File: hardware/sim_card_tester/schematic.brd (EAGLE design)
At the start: 160 x 101.6 mm, 140 parts, among them IC1 TPS6300, J1 CON_MICRO_SDDM3AT-SF-PEJM5, J2 MICRO_USB_B_HIROSE_ZX62R-B-5P, J3 NANO_SIM, J4 NANO_SIM, J5 NANO_SIM, J6 NANO_SIM, J7 TC2030-JLINK-L, J8 U.FL-R-SMT, Q1 MOSFET-NCHANNELSMD, Q2 MOSFET-NCHANNELSMD, Q3 MOSFET-NCHANNELSMD, Q4 SI223DDS, U1 AB1815-T3, U10 SIP32510, U11 SIP32510, U12 UBLOX_SARA_G350, U13 TXB0104RUT, U15 MAX4734EUB+, U2 BGA725L6-ALT, U20 MAX4734EUB+, U21 MAX4734EUB+, U22 MAX4734EUB+, U3 FTDI234XD, U4 SAFFB1G56KB0F0A, U5 MAX8887EZK33+T, U6 MCP73831, U7 MAX-M8, U8 MAX67XXMAX6749MAX67XX, U9 NRF52840, X1 ABS07-32.768KHZ-7-T, X4 32MHz, X5 32.768kHz

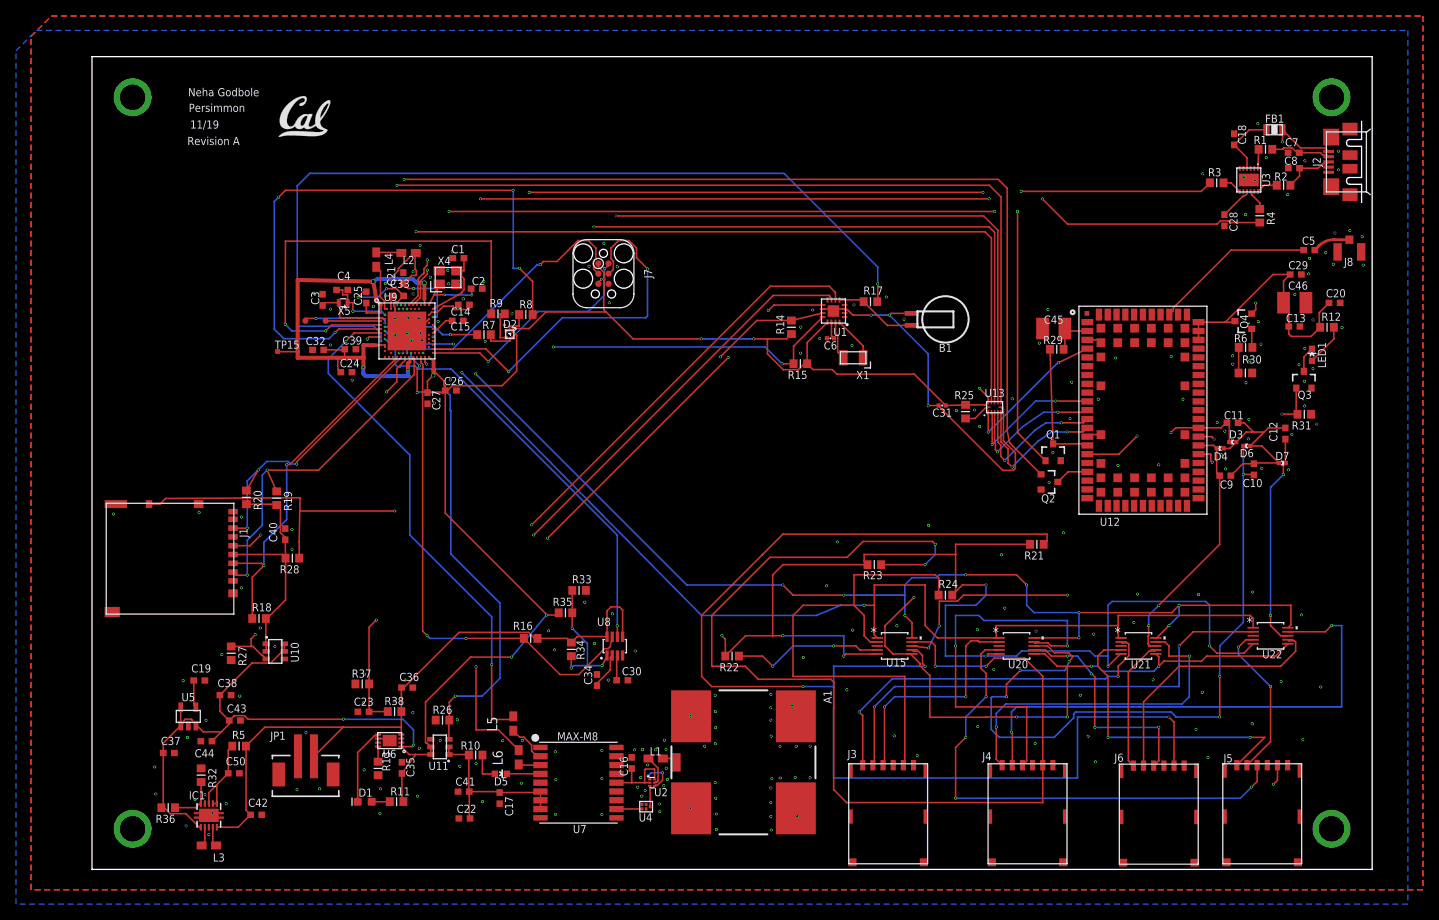
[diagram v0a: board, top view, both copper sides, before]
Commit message: fixed numbering
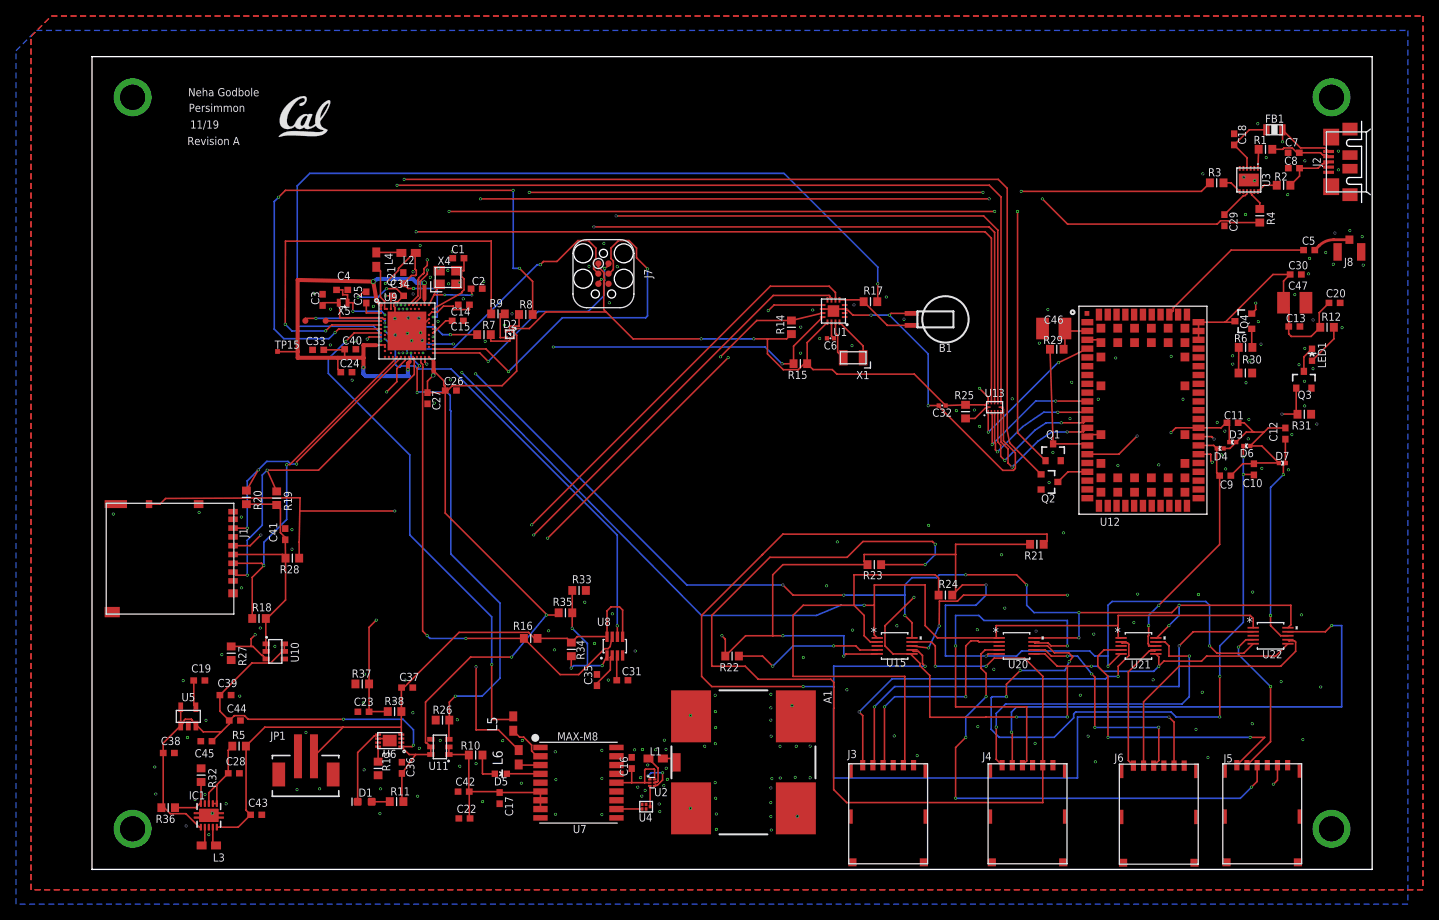
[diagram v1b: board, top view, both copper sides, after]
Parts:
- removed C50: .1uF, Nordic_nRF:RESC0603_L
- added C47: 220uF, BeagleBone_Black_Wireless:C1210
- C28: value 100nF -> .1uF
- C30: value 0.82uF -> 100nF
- C31: value 1uF -> 0.82uF; device passives:0402_CAP -> Nordic_nRF:RESC0603_L
- C32: device Nordic_nRF:RESC0603_L -> passives:0402_CAP
- C34: value 2.2uF -> 1uF
- C35: value 4.7uF -> 2.2uF
- C41: value 10uF -> 4.7uF
- C45: value 100uF -> 10uF; device BeagleBone_Black_Wireless:C1210 -> Nordic_nRF:RESC0603_L
- C46: value 220uF -> 100uF
- moved C28 141.8 mm to (17.7, 12.0), turned to 0 degrees
- moved C45 117.8 mm to (14.3, 16.0)
- moved C30 98.3 mm to (150.5, 74.4)
- moved C32 78.3 mm to (106.3, 58.0)
- moved C34 54.1 mm to (38.3, 71.7), turned to 0 degrees
- moved C31 52.7 mm to (66.3, 23.6), turned to 0 degrees
- moved C39 46.0 mm to (16.7, 21.8)
- moved C41 39.2 mm to (24.2, 41.9), turned to 90 degrees
- moved C37 30.9 mm to (39.4, 22.7)
- moved C46 30.3 mm to (120.2, 67.6), turned to 180 degrees
- moved C35 26.7 mm to (63.1, 23.7)
- moved C42 26.1 mm to (46.5, 9.73)
- moved C40 24.5 mm to (32.3, 65.0), turned to 0 degrees
- moved C43 12.1 mm to (20.5, 6.83)
- moved C33 12.1 mm to (28.3, 64.9), turned to 180 degrees
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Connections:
- net +3V3: now also C33.1, C36.1, C40.1, C45.1; no longer C31.1, C35.1, C37.1, C43.1
- net BAT: now also C37.1, C43.1; no longer C36.1, C42.1
- net GND: now also C41.2, C42.1, C47.2; no longer C41.1, C42.2, C50.2
- net GPS_VCC: now also C42.2; no longer C41.2
- net GSM_GATED: now also C30.1, C47.1; no longer C29.1, C46.1
- net N$16: now also C46.1; no longer C45.1
- net N$29: now also C28.1; no longer C50.1
- net N$32: now also C34.1; no longer C33.1
- net N$36: now also C31.1; no longer C30.1
- net N$39: now also C35.1; no longer C34.1
- net N$55: now also C41.1; no longer C40.1
- net VCC_LINUX_1V8: now also C29.1; no longer C28.1

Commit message: cleaned up wires
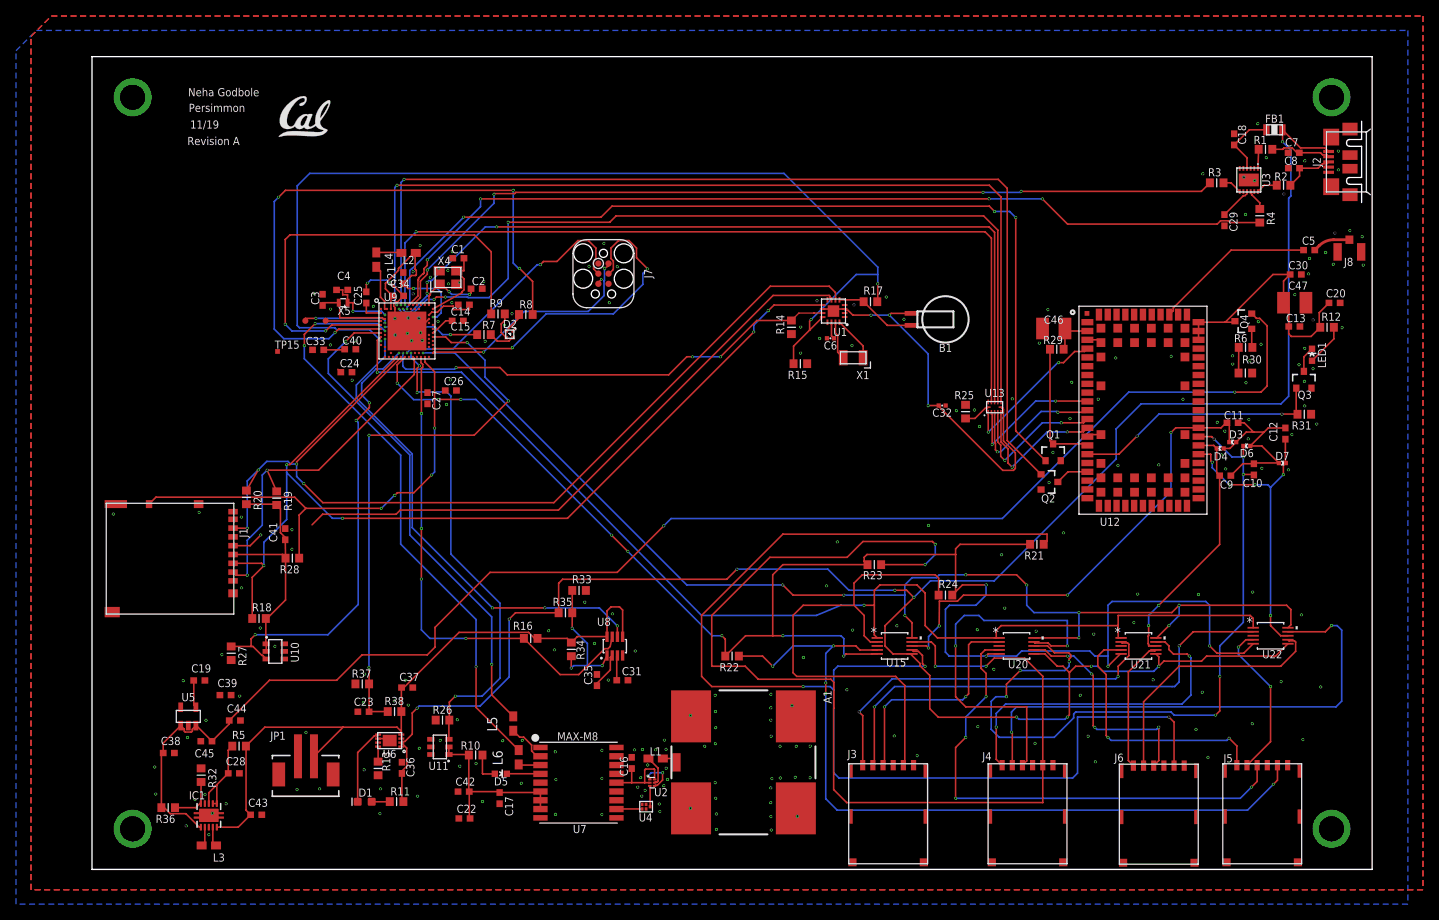
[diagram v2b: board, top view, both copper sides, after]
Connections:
- removed net +3V3: C24.1, C26.1, C27.1, C32.1, C33.1, C36.1, C38.1, C39.1, C40.1, C44.1, C45.1, D2.1, IC1.1, J7.1, Q4.2, R11.2, R14.1, R15.1, R25.2, R35.1, R36.2, TP15.TP, U1.13, U10.5, U10.6, U11.5, U11.6, U13.11, U5.1, U5.3, U5.5, U6.1, U6.2, U9.A22, U9.AD14, U9.AD23, U9.B1, U9.W1, U9.Y2
- removed net VCC_LINUX_1V8: C29.1, U3.9
- new net 5V: C36.1, FB1.P$2, J2.1, R11.2, R35.1, U15.6, U20.6, U21.6, U22.6, U6.1, U6.2
- new net VCCA: C38.1, C44.1, C45.1, IC1.1, Q4.2, R36.2, U5.1, U5.3
- net VCC: now also C24.1, C26.1, C27.1, C29.1, C32.1, C33.1, C39.1, C40.1, D2.1, J7.1, R14.1, R15.1, R25.2, TP15.TP, U1.13, U10.5, U10.6, U11.5, U11.6, U13.11, U3.9, U5.5, U9.A22, U9.AD14, U9.AD23, U9.B1, U9.W1, U9.Y2; no longer FB1.P$2, J2.1, U15.6, U20.6, U21.6, U22.6
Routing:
- net +3V3: track 364.0 -> 0.00 mm, vias 13 -> 0
- net 5V: track 0.00 -> 271.1 mm, vias 0 -> 10
- net VCCA: track 0.00 -> 185.0 mm, vias 0 -> 2
- net VCC: track 164.1 -> 8.63 mm, vias 6 -> 0
- net !RTC_CS: track 171.8 -> 130.5 mm, vias 4 -> 3
- net BATIN: track 52.8 -> 70.3 mm, vias 2 -> 4
- net GPS_RXD: track 65.3 -> 74.1 mm, vias 3 -> 4
- net WDI: track 53.1 -> 60.1 mm, vias 2 -> 4
- net NRF_SCK: track 88.1 -> 81.2 mm, vias 2 -> 1
- net SD_EN: track 49.4 -> 56.3 mm, vias 2 -> 4
- net IO3: track 38.4 -> 33.1 mm
- net NRF_SWDCLK: track 47.6 -> 42.6 mm
- net NRF_MISO: track 124.1 -> 119.5 mm
- net VCC_LINUX_1V8: track 4.16 -> 0.00 mm
- net MUX_SEL1: track 148.7 -> 144.6 mm, vias 3 -> 2
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- added copper zone on layer 15, net VCC

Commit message: added test points
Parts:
- added TP1, TP10, TP11, TP12, TP16, TP17, TP18, TP19, TP2, TP20, TP21, TP22, TP23, TP24, TP25, TP26, TP27, TP28, TP29, TP3, TP30, TP4, TP5, TP6, TP7, TP8, TP9: TEST-POINT, headers:PAD.03X.03
- added TP31: TPTP06SQ, testpad:TP06SQ
- TP15: value TPTP06SQ -> TEST-POINT; device testpad:TP06SQ -> headers:PAD.03X.03
- moved TP15 48.6 mm to (70.2, 77.0)
- moved TP13 32.2 mm to (57.3, 78.4)
- moved TP14 23.5 mm to (52.2, 63.7)
- moved J5 5.13 mm to (141.1, 6.96)
- moved J6 3.76 mm to (129.6, 6.91)
- moved J2 3.49 mm to (160.0, 85.2)
- moved R36 3.35 mm to (10.6, 10.9), turned to 270 degrees
- moved C18 2.42 mm to (142.1, 89.0)
- moved C29 2.42 mm to (140.8, 78.8)
- moved C8 2.42 mm to (149.5, 85.3)
- moved FB1 2.42 mm to (147.1, 90.1)
- moved C7 2.42 mm to (149.5, 87.3)
- moved R1 2.42 mm to (146.0, 87.7)
- moved R3 2.42 mm to (139.9, 83.5)
- moved R2 2.42 mm to (148.2, 83.2)
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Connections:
- net !EXTERNAL_RST: now also TP12.P$1
- net !NRF_CS_SD: now also TP11.P$1
- net !NRF_RST: now also TP13.P$1
- net !RTC_CS: now also TP4.P$1
- net !RTC_INT1: now also TP8.P$1
- net !SD_DETECT: now also TP21.P$1
- net BATIN: now also TP22.P$1
- net GND: now also TP28.P$1
- net GPS_PWR_EN: now also TP10.P$1
- net GPS_RXD: now also TP1.P$1
- net GPS_TXD: now also TP2.P$1
- net GSM_CTS: now also TP16.P$1
- net GSM_POWER: now also TP17.P$1
- net GSM_RST: now also TP19.P$1
- net GSM_RTS: now also TP18.P$1
- net GSM_TX: now also TP20.P$1
- net MUX_EN: now also TP9.P$1
- net MUX_SEL1: now also TP23.P$1
- net MUX_SEL2: now also TP26.P$1
- net NRF_GPIO_0: now also TP29.P$1; no longer TP13.P$1
- net NRF_GPIO_1: now also TP30.P$1; no longer TP14.P$1
- net NRF_MISO: now also TP7.P$1
- net NRF_MOSI: now also TP5.P$1
- net NRF_SWDCLK: now also TP15.P$1
- net NRF_SWDIO: now also TP14.P$1
- net SD_EN: now also TP6.P$1
- net UART_RX: now also TP24.P$1
- net UART_TX: now also TP25.P$1
- net VCC: now also TP27.P$1, TP31.TP; no longer TP15.TP
- net WDI: now also TP3.P$1
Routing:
- net VCC: track 8.63 -> 46.1 mm, vias 0 -> 19
- net VCC4: track 157.0 -> 141.6 mm
- net GND: track 75.6 -> 87.7 mm, vias 242 -> 236
- net NRF_SCK: track 81.2 -> 89.6 mm, vias 1 -> 4
- net IO3: track 33.1 -> 27.6 mm
- net RST4: track 28.6 -> 23.3 mm
- net RST3: track 63.0 -> 58.3 mm
- net VCC3: track 99.1 -> 94.8 mm
- net NRF_SWDIO: track 28.7 -> 32.3 mm
- net !SD_DETECT: track 60.0 -> 63.3 mm
- net GPS_PWR_EN: track 60.1 -> 63.3 mm
- net NRF_MOSI: track 125.3 -> 128.4 mm
- net GPS_TXD: track 62.2 -> 65.3 mm
- net BATIN: track 70.3 -> 73.2 mm
- net !RTC_CS: track 130.5 -> 133.2 mm
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
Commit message: updated bom
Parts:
- C29, C30: value 100nF -> .1uF
- C32, C6: device passives:0402_CAP -> Nordic_nRF:RESC0603_L
- moved C32 15.2 mm to (91.5, 61.4), turned to 0 degrees
- moved C6 2.03 mm to (91.8, 64.4)
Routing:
- net VCC: track 46.1 -> 48.3 mm
- net N$13: track 2.13 -> 3.97 mm
- net GND: track 87.7 -> 87.6 mm, vias 236 -> 237
